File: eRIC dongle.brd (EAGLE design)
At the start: 20.8 x 41.3 mm, 43 parts

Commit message: tantalum annotation
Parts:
- C3: value 10uF -> 10uF tantalum
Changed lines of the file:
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@@
 <element name="E$2" library="adafruit" package="R0603" value="27ohm" x="19.65" y="16.05" rot="R90"/>
 <element name="E$3" library="adafruit" package="R0603" value="27ohm" x="17.6" y="16.05" rot="R90"/>
-<element name="C3" library="SparkFun" package="EIA3216" value="10uF" x="26.3542" y="23.2008" smashed="yes">
+<element name="C3" library="SparkFun" package="EIA3216" value="10uF tantalum" x="26.3542" y="23.2008" smashed="yes">
 <attribute name="NAME" x="23.8142" y="24.5818" size="0.4064" layer="25"/>
 <attribute name="VALUE" x="25.8732" y="24.1518" size="0.4064" layer="27"/>

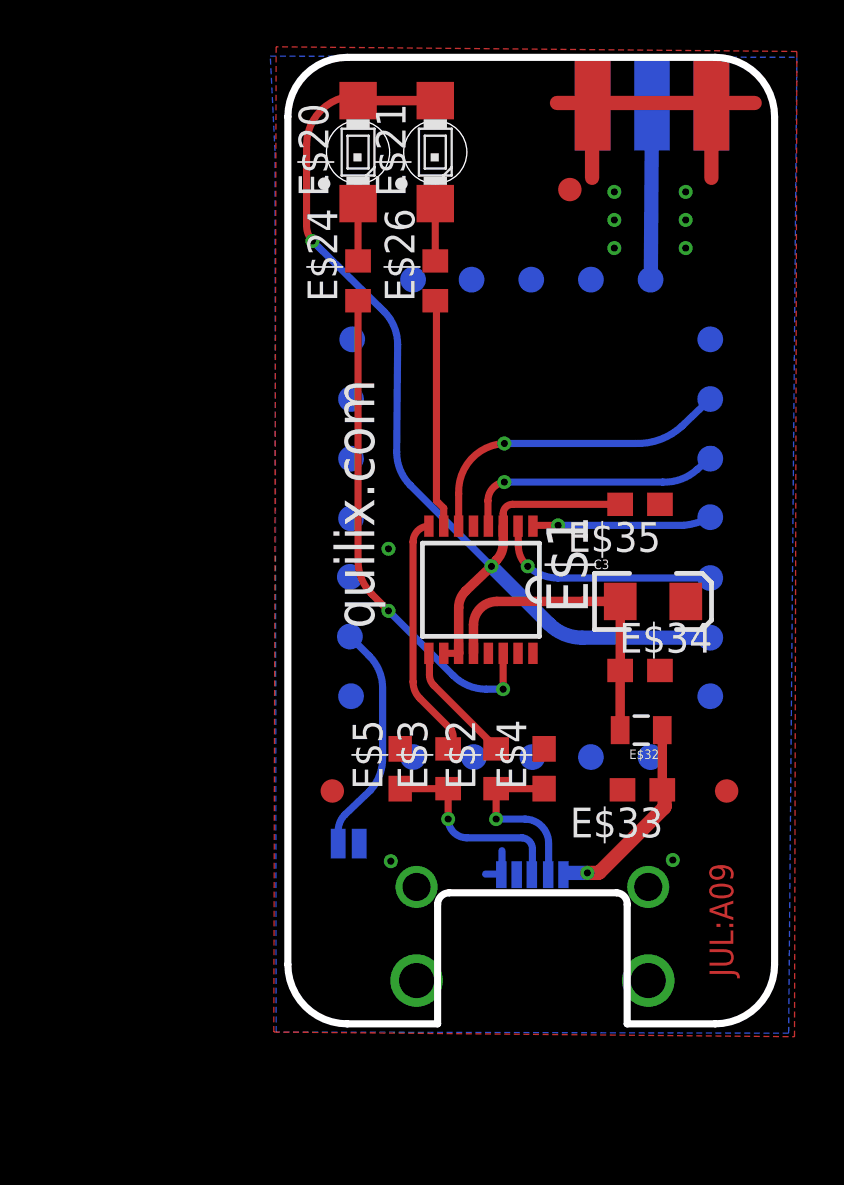
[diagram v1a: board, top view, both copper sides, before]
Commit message: component placement, updated BOM, and refresh to production archive
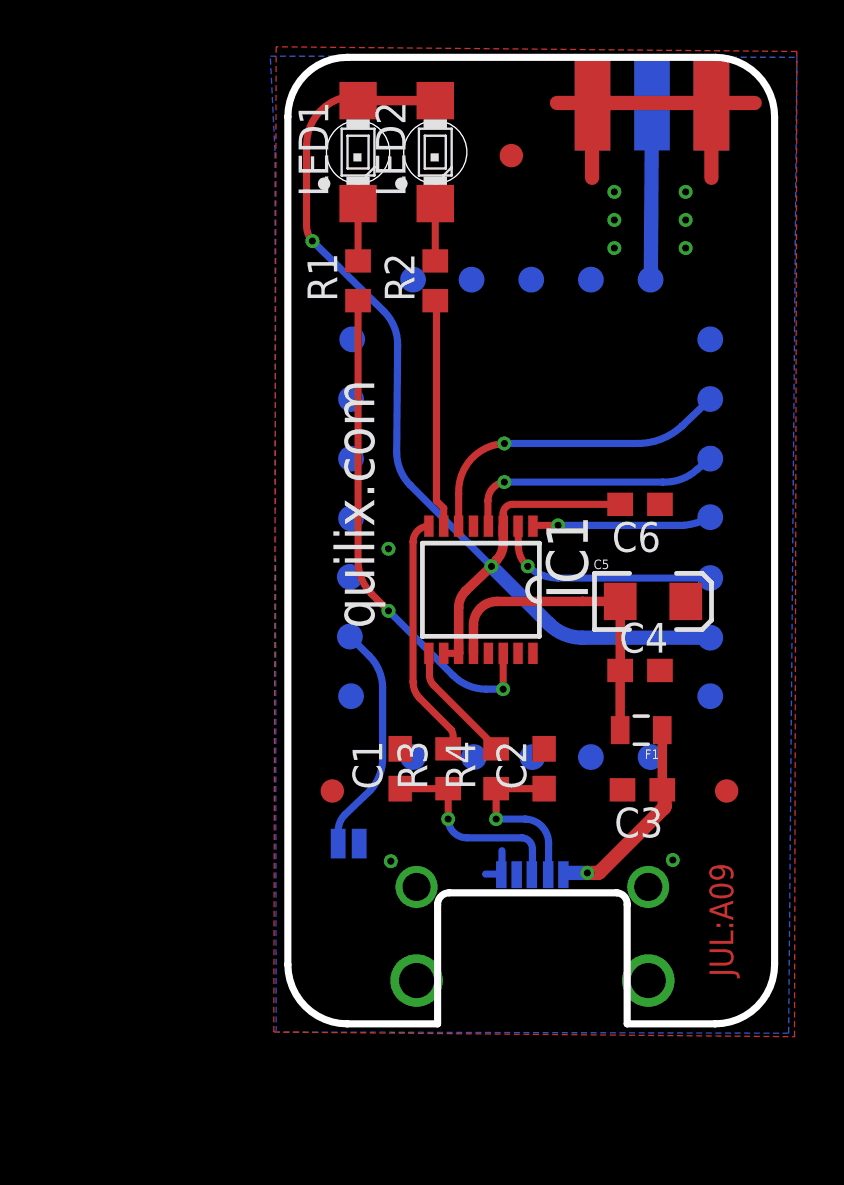
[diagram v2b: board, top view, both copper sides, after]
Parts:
- removed E$33: 10nF, adafruit:C0603
- added C5: 10uF tantalum, SparkFun:EIA3216
- C3: value 10uF tantalum -> 10nF; device SparkFun:EIA3216 -> adafruit:C0603
- SMA: value (none) -> SMA-PCB
- moved C3 8.06 mm to (25.9, 15.2), turned to 180 degrees
- moved E$30 2.89 mm to (20.3, 42.2)
- renumbered E$1 to IC1, E$2 to R4, E$20 to LED1, E$21 to LED2, E$24 to R1, E$26 to R2, E$3 to R3, E$32 to F1, E$34 to C4, E$35 to C6, E$4 to C2, E$5 to C1, GND2 to SMA
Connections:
- net GND: now also C3.2, C5.A; no longer C3.A, E$33.2
- net S$10: now also C5.C; no longer C3.C
- net S$31: now also C3.1; no longer E$33.1

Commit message: goof on silkscreen - tant cap 180 out
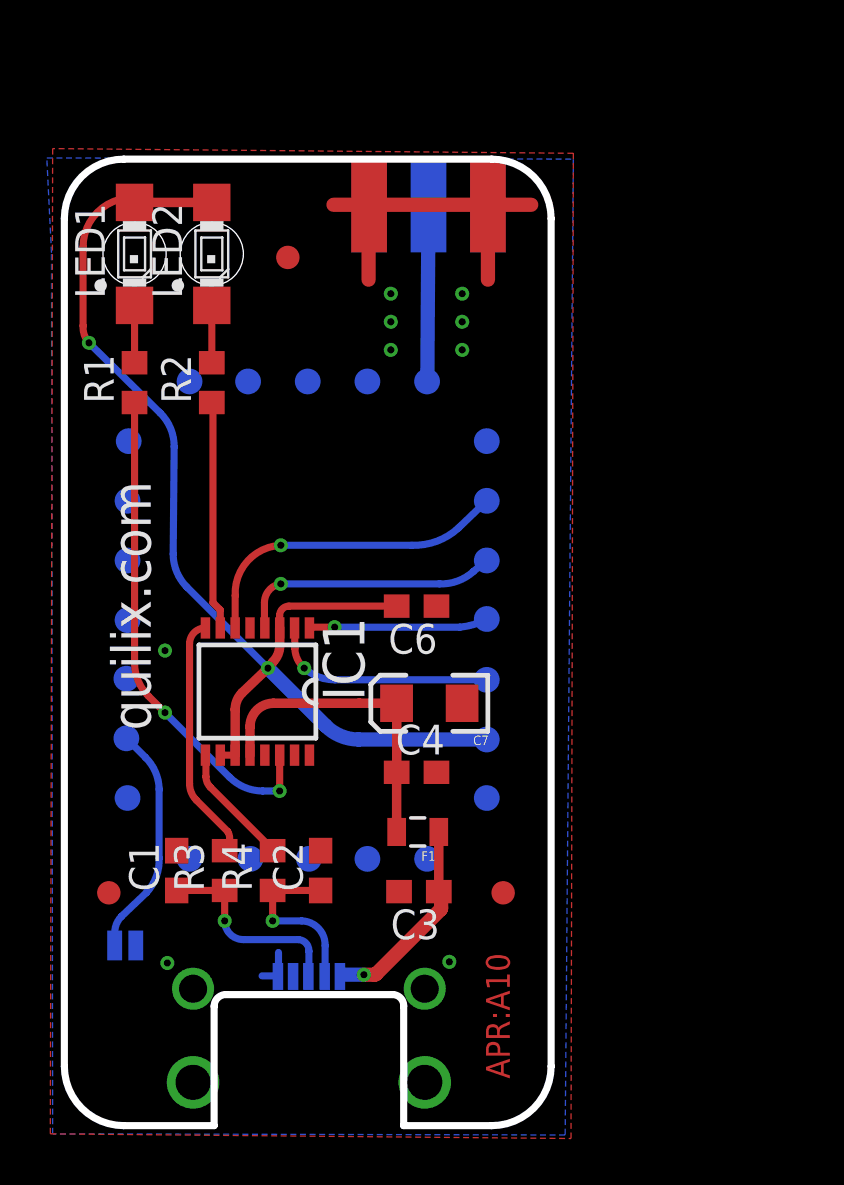
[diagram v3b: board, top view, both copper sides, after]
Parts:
- removed C5: 10uF tantalum, SparkFun:EIA3216
- added C7: 10uF tantalum, SparkFun:EIA3216
- moved C1 10.5 mm to (6.00, 11.7)
- moved C6 10.5 mm to (16.2, 23.0)
- moved E$11 10.5 mm to (16.7, 32.6)
- moved E$15 10.5 mm to (6.55, 32.6)
- moved E$25 10.5 mm to (16.7, 12.2)
- moved E$29 10.5 mm to (6.55, 12.2)
- moved E$30 10.5 mm to (10.8, 37.9)
- moved E$31 10.5 mm to (9.05, 32.6)
- moved E$7 10.5 mm to (19.2, 27.5)
- moved E$8 10.5 mm to (3.85, 19.9)
- moved LED1 10.5 mm to (4.20, 38.0)
- moved LED2 10.5 mm to (7.50, 38.0)
- moved R1 10.5 mm to (4.20, 32.5)
- moved R2 10.5 mm to (7.50, 32.5)
- moved R3 10.5 mm to (8.05, 11.7)
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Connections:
- net GND: now also C7.C; no longer C5.A
- net S$10: now also C7.A; no longer C5.C
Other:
- board text added: "APR:A10"
- board text removed: "JUL:A09"

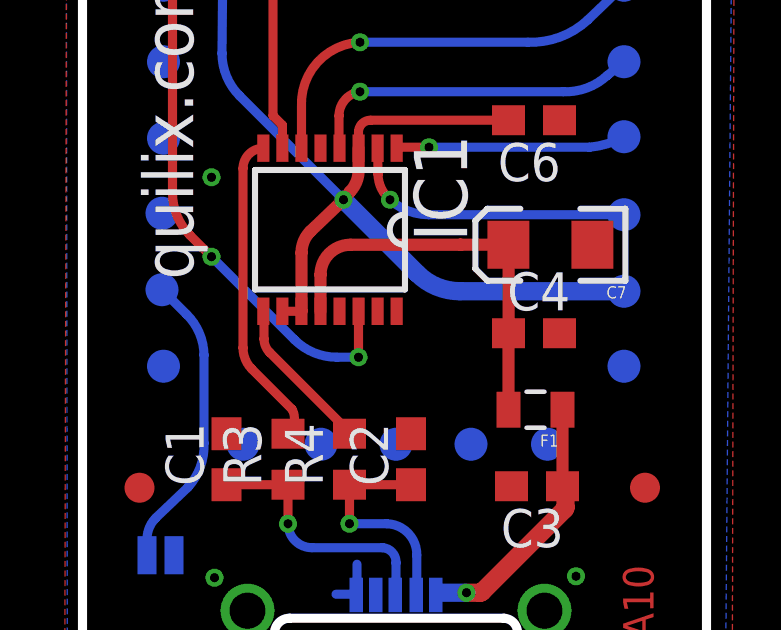
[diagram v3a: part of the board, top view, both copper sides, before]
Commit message: CBUS3 sleep jumper added
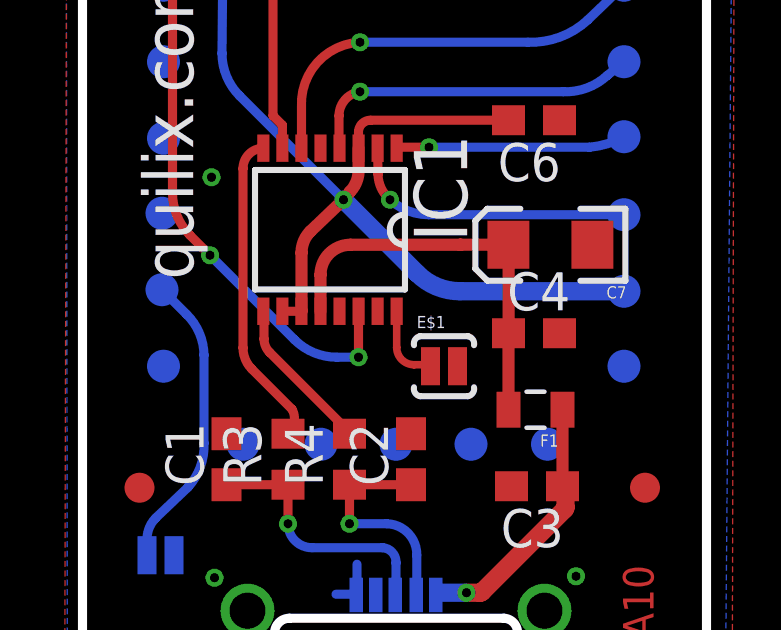
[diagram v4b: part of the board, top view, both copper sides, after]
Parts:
- added E$1: (no value), SparkFun-Capacitors:SJ_2S-NO
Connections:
- new net S$29: E$1.1, IC1.16
- net GND: now also E$1.2
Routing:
- net S$29: track 0.00 -> 2.59 mm
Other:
- board text added: "C3"
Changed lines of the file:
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@@
 <layer number="25" name="tNames" color="7" fill="1" visible="no" active="yes"/>
 <layer number="26" name="bNames" color="7" fill="1" visible="no" active="yes"/>
-<layer number="27" name="tValues" color="7" fill="1" visible="yes" active="yes"/>
-<layer number="28" name="bValues" color="7" fill="1" visible="yes" active="yes"/>
+<layer number="27" name="tValues" color="7" fill="1" visible="no" active="yes"/>
+<layer number="28" name="bValues" color="7" fill="1" visible="no" active="yes"/>
 <layer number="29" name="tStop" color="7" fill="3" visible="no" active="yes"/>
 <layer number="30" name="bStop" color="7" fill="6" visible="no" active="yes"/>
@@
 <wire x1="1.2" y1="3.34" x2="3.74" y2="0.8" width="0.3048" layer="20" curve="90"/>
 <wire x1="3.74" y1="0.8" x2="7.6" y2="0.8" width="0.3048" layer="20"/>
+<text x="12.635" y="16.26" size="1.27" layer="122" font="vector" ratio="15" rot="MR90">C3</text>
 </plain>
 <attributes>
@@
 <attribute name="VALUE" x="17.2768" y="17.8982" size="0.4064" layer="27" rot="R180"/>
 </element>
+<element name="E$1" library="SparkFun-Capacitors" package="SJ_2S-NO" value="" x="13.25" y="14.8"/>
 </elements>
 <signals>
@@
 <wire x1="10.4" y1="15.1" x2="9.678428125" y2="15.1" width="0.3048" layer="16"/>
 <wire x1="9.678428125" y1="15.1" x2="8.2642125" y2="15.6857875" width="0.3048" layer="16" curve="-45.000063"/>
-<wire x1="8.2642125" y1="15.6857875" x2="5.5" y2="18.45" width="0.3048" layer="16"/>
-<via x="5.5" y="18.45" extent="1-16" drill="0.3"/>
-<wire x1="5.5" y1="18.45" x2="4.7857875" y2="19.1642125" width="0.3048" layer="1"/>
+<wire x1="8.2642125" y1="15.6857875" x2="5.45" y2="18.5" width="0.3048" layer="16"/>
+<via x="5.45" y="18.5" extent="1-16" drill="0.3"/>
+<wire x1="5.45" y1="18.5" x2="4.7857875" y2="19.1642125" width="0.3048" layer="1"/>
 <wire x1="4.7857875" y1="19.1642125" x2="4.2" y2="20.578428125" width="0.3048" layer="1" curve="-45.00009"/>
 <wire x1="4.2" y1="20.578428125" x2="4.2" y2="31.7" width="0.3048" layer="1"/>
@@
 <via x="5.5" y="21.1" extent="1-16" drill="0.3"/>
 <contactref element="C7" pad="C"/>
+<contactref element="E$1" pad="2"/>
 </signal>
 <signal name="S$22">
@@
 <wire x1="11.34289375" y1="9.55" x2="10.1" y2="9.55" width="0.3048" layer="16"/>
 </signal>
+<signal name="S$29">
+<contactref element="E$1" pad="1"/>
+<contactref element="IC1" pad="16"/>
+<wire x1="11.6725" y1="16.6322" x2="11.6725" y2="15.4275" width="0.254" layer="1"/>
+<wire x1="11.6725" y1="15.4275" x2="12.25" y2="14.85" width="0.254" layer="1" curve="90"/>
+<wire x1="12.25" y1="14.85" x2="12.75" y2="14.85" width="0.254" layer="1"/>
+<wire x1="12.75" y1="14.85" x2="12.8" y2="14.8" width="0.254" layer="1" curve="-90"/>
+</signal>
 </signals>
